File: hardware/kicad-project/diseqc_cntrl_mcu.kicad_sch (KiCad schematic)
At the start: 38 parts, among them IC2 STM32F407VGT6, IC3 USBLC6-2P6, J2 Conn_01x04_Pin, J3 Conn_01x04_Pin, J4 USB4110-GF-A, J5 SWD, Y1 8MHZ

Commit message: Corrective changes to power regulation: F1, PS1
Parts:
- C11, C12, C14, C16, C17, C19, C20, C9, R10, R11, R14, R15, R9: My Stock 50 -> (none)
- C13, C15, C18: My Stock 25 -> (none)
- IC2: footprint STM32:QFP50P1600X1600X160-100N -> diseqc_cntrl:QFP50P1600X1600X160-100N
- IC3: footprint USBCL6:USBLC62P6 -> diseqc_cntrl:USBLC62P6
- J4: footprint USB4110GFA -> diseqc_cntrl:USB4110GFA
- J5: footprint HDRV10W64P254_2X5_1270X495X838P -> diseqc_cntrl:HDRV10W64P254_2X5_1270X495X838P
- NT1: My Stock 1000 -> (none)
- R12, R7, R8: My Stock 0 -> (none)
- R13, R6: My Stock 100 -> (none)
- S1: footprint PCM12SMTBR -> diseqc_cntrl:PCM12SMTBR
- Y1: footprint ABLS 8mhz xtal:ABLS8000MHz20B3HT -> diseqc_cntrl:ABLS8000MHz20B3HT

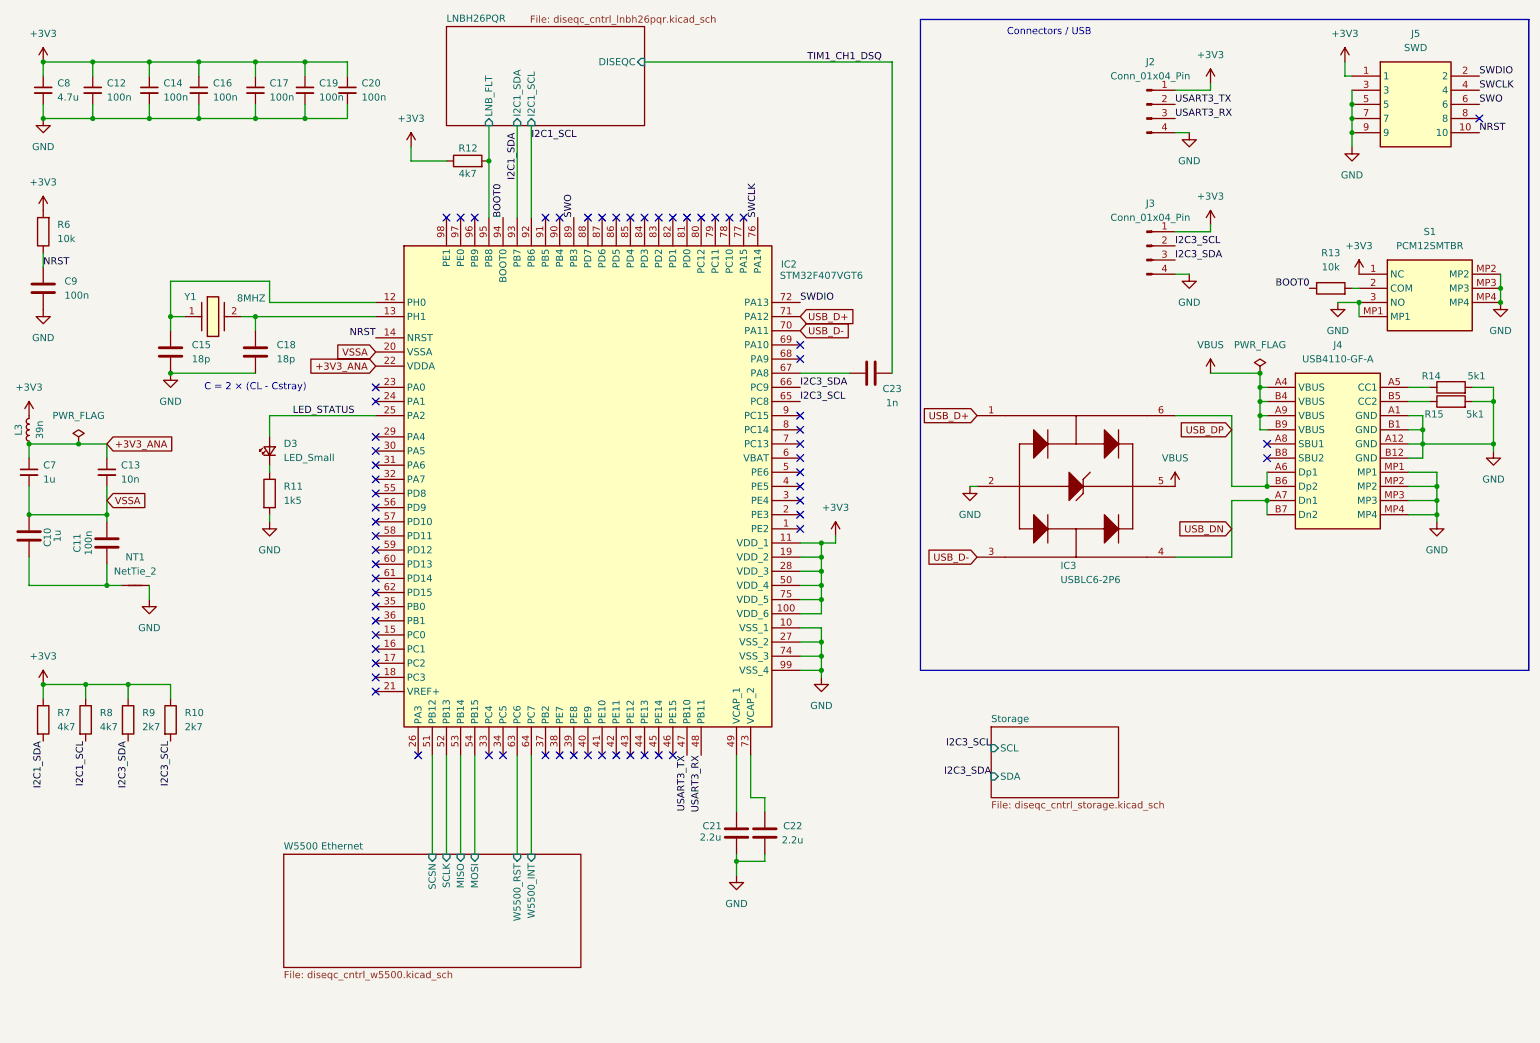
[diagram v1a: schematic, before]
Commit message: Added more test points
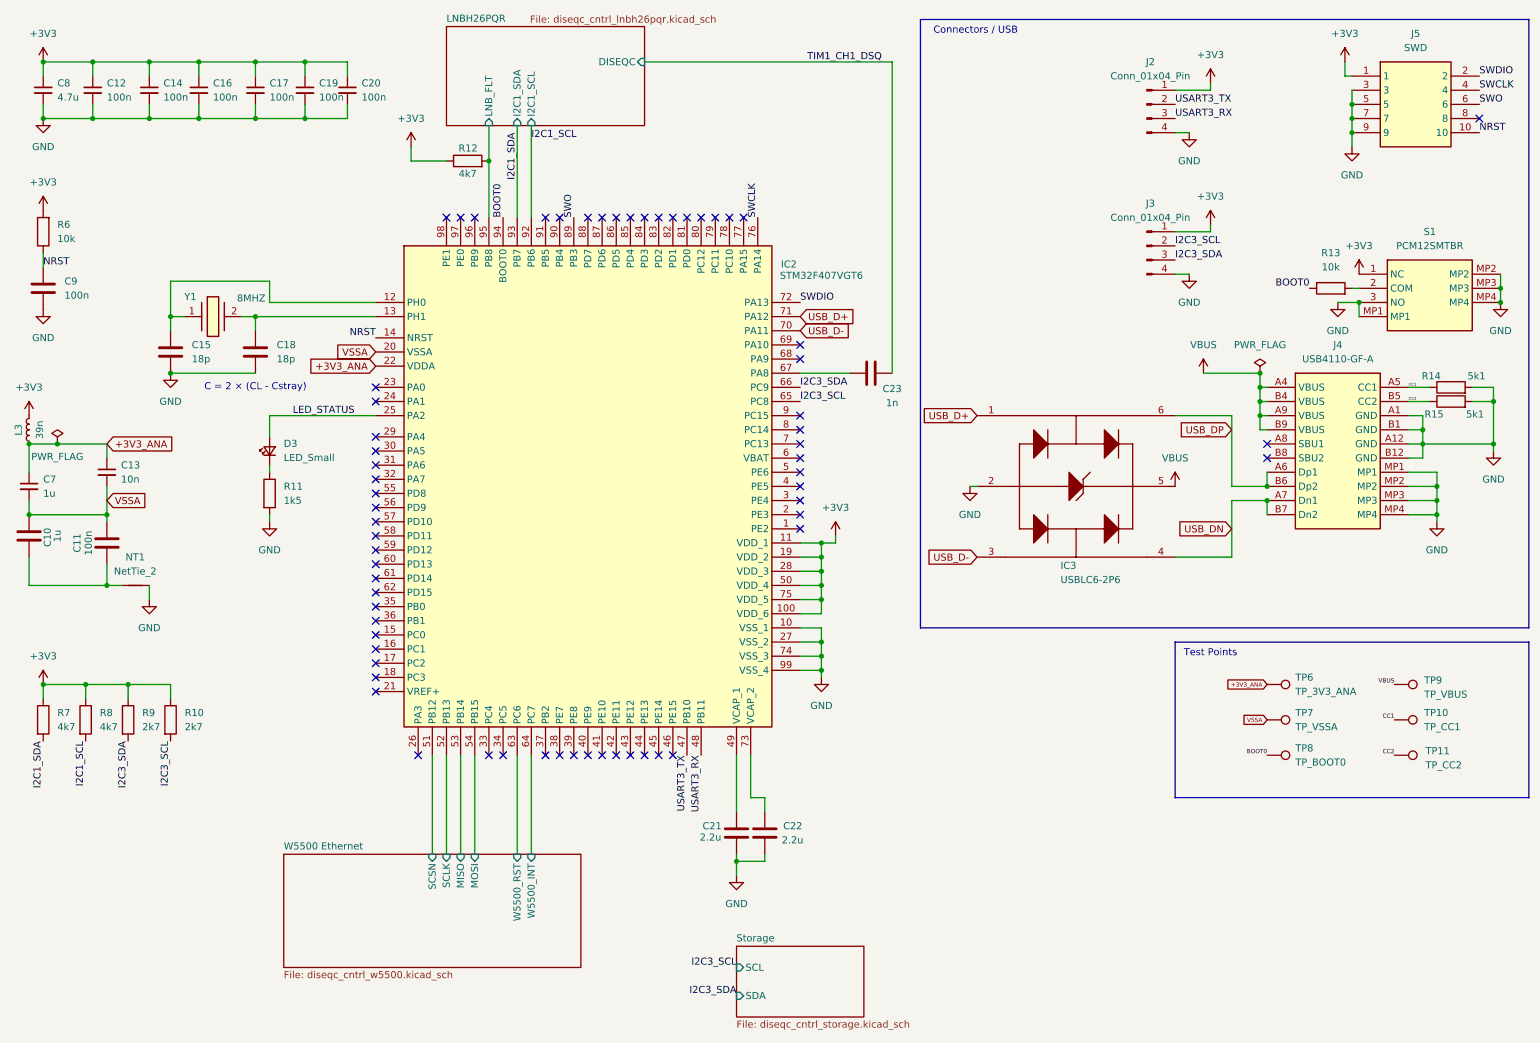
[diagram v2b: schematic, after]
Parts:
- added TP10: TP_CC1, TestPoint:TestPoint_THTPad_D1.0mm_Drill0.5mm, symbol Connector:TestPoint
- added TP11: TP_CC2, TestPoint:TestPoint_THTPad_D1.0mm_Drill0.5mm, symbol Connector:TestPoint
- added TP6: TP_3V3_ANA, TestPoint:TestPoint_THTPad_D1.0mm_Drill0.5mm, symbol Connector:TestPoint
- added TP7: TP_VSSA, TestPoint:TestPoint_THTPad_D1.0mm_Drill0.5mm, symbol Connector:TestPoint
- added TP8: TP_BOOT0, TestPoint:TestPoint_THTPad_D1.0mm_Drill0.5mm, symbol Connector:TestPoint
- added TP9: TP_VBUS, TestPoint:TestPoint_THTPad_D1.0mm_Drill0.5mm, symbol Connector:TestPoint
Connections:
- net +3V3_ANA: now also TP6.1
- net BOOT0: now also TP8.1
- net VBUS: now also TP9.1
- net VSSA: now also TP7.1
- net CC1: now reaches J4.A5 (CC1), R14.1
- net CC1: now also TP10.1
- net CC2: now reaches J4.B5 (CC2), R15.1
- net CC2: now also TP11.1
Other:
- note added: "Test Points"
- moved on the sheet: C7

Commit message: Fixed pin conflict: TIM1_CH1/I2C3_SCL
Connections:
- net TIM1_CH1_DSQ is gone; now on net TIM4_CH1: C23.2
- net I2C3_SCL: now also IC2.67 (PA8); no longer IC2.65 (PC8)
- net LNBH26PQR/DISEQC: now reaches C23.1
- net LNBH26PQR/DISEQC: no longer IC2.67 (PA8)
- net TIM4_CH1: now reaches IC2.59 (PD12)
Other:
- moved on the sheet: C23
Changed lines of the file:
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@@
 	)
 	(no_connect
-		(at 77.47 110.49)
-	)
-	(no_connect
 		(at 77.47 123.19)
 	)
@@
 	)
 	(no_connect
+		(at 153.67 83.82)
+	)
+	(no_connect
 		(at 125.73 50.8)
 	)
@@
 	(wire
 		(pts
-			(xy 170.18 22.86) (xy 125.73 22.86)
-		)
-		(stroke
-			(width 0)
-			(type default)
-		)
-	)
-	(wire
-		(pts
 			(xy 36.83 22.86) (xy 36.83 25.4)
 		)
@@
 	(wire
 		(pts
-			(xy 170.18 78.74) (xy 170.18 22.86)
-		)
-		(stroke
-			(width 0)
-			(type default)
-		)
-	)
-	(wire
-		(pts
 			(xy 236.22 86.36) (xy 237.49 86.36)
 		)
@@
 	(wire
 		(pts
-			(xy 153.67 78.74) (xy 162.56 78.74)
-		)
-		(stroke
-			(width 0)
-			(type default)
-		)
-	)
-	(wire
-		(pts
 			(xy 227.33 27.94) (xy 227.33 26.67)
 		)
@@
 	(wire
 		(pts
+			(xy 125.73 22.86) (xy 129.54 22.86)
+		)
+		(stroke
+			(width 0)
+			(type default)
+		)
+	)
+	(wire
+		(pts
 			(xy 262.89 104.14) (xy 267.97 104.14)
 		)
@@
 		)
 	)
+	(label "TIM4_CH1"
+		(at 77.47 110.49 180)
+		(effects
+			(font
+				(size 1.27 1.27)
+			)
+			(justify right bottom)
+		)
+	)
 	(label "SWCLK"
 		(at 146.05 50.8 90)
@@
 		)
 	)
-	(label "TIM1_CH1_DSQ"
-		(at 154.94 22.86 0)
+	(label "TIM4_CH1"
+		(at 137.16 22.86 0)
 		(effects
 			(font
@@
 		)
 	)
+	(label "I2C3_SCL"
+		(at 153.67 78.74 0)
+		(effects
+			(font
+				(size 1.27 1.27)
+			)
+			(justify left bottom)
+		)
+	)
 	(label "SWCLK"
 		(at 275.59 27.94 0)
@@
 		)
 	)
-	(label "I2C3_SCL"
-		(at 153.67 83.82 0)
-		(effects
-			(font
-				(size 1.27 1.27)
-			)
-			(justify left bottom)
-		)
-	)
 	(label "I2C1_SCL"
 		(at 25.4 144.78 270)
@@
 	(symbol
 		(lib_id "diseqc_cntrl:C")
-		(at 166.37 78.74 90)
+		(at 133.35 22.86 90)
 		(unit 1)
 		(exclude_from_sim no)
@@
 		(dnp no)
 		(property "Reference" "C23"
-			(at 170.18 81.534 90)
+			(at 133.35 26.67 90)
 			(effects
 				(font
@@
 		)
 		(property "Value" "1n"
-			(at 170.18 84.074 90)
+			(at 133.604 28.956 90)
 			(effects
 				(font
@@
 		)
 		(property "Footprint" "Capacitor_SMD:C_0603_1608Metric_Pad1.08x0.95mm_HandSolder"
-			(at 170.18 77.7748 0)
+			(at 137.16 21.8948 0)
 			(effects
 				(font
@@
 		)
 		(property "Datasheet" "https://www.mouser.co.uk/datasheet/3/76/1/GRM188R71H102KA01-01.pdf"
-			(at 166.37 78.74 0)
+			(at 133.35 22.86 0)
 			(effects
 				(font
@@
 		)
 		(property "Description" "Unpolarized capacitor"
-			(at 166.37 78.74 0)
+			(at 133.35 22.86 0)
 			(effects
 				(font
@@
 		)
 		(property "Maufacturer_Part_Number" ""
-			(at 166.37 78.74 90)
+			(at 133.35 22.86 90)
 			(effects
 				(font
@@
 		)
 		(property "Manufacturer_Part_Code" ""
-			(at 166.37 78.74 90)
+			(at 133.35 22.86 90)
 			(effects
 				(font
@@
 		)
 		(property "Mouser_Part_Number" ""
-			(at 166.37 78.74 90)
+			(at 133.35 22.86 90)
 			(effects
 				(font
@@
 		)
 		(property "Mouser Part Number" "81-GRM39X102K050"
-			(at 166.37 78.74 90)
+			(at 133.35 22.86 90)
 			(effects
 				(font
@@
 		)
 		(instances
-			(project ""
+			(project "diseqc_cntrl"
 				(path "/82a905d8-f1d7-4995-9c16-94cf3cdcaad9/65fcf1a0-d0f2-4bf0-9977-67dd9f84afa5"
 					(reference "C23")

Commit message: Moved SWD to TC2050 connector
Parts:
- removed J5: SWD, diseqc_cntrl:HDRV10W64P254_2X5_1270X495X838P, symbol diseqc_cntrl:TSW-105-23-T-D
- added J9: Conn_ARM_SWD_TagConnect_TC2030, Connector:Tag-Connect_TC2050-IDC-NL_2x05_P1.27mm_Vertical, symbol Connector:TC2050
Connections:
- net +3V3: now also J9.1
- net GND: now also J9.3, J9.5, J9.8, J9.9
- net NRST: now also J9.10
- net SWCLK: now also J9.4
- net SWDIO: now also J9.2
- net SWO: now also J9.6
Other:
- moved on the sheet: J2

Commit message: Fix: Add VBUS sense to MCU for USB DFU
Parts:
- added R31: 100k, Resistor_SMD:R_0603_1608Metric_Pad0.98x0.95mm_HandSolder, symbol diseqc_cntrl:R
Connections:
- net +3V3: now also IC2.6 (VBAT)
- net VBUS: now also R31.2
- net VBUS_SENSE: now reaches IC2.68 (PA9)
- net VBUS_SENSE: now also R31.1
- no-connect marks 65 -> 63
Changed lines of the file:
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@@
 	)
 	(no_connect
-		(at 153.67 76.2)
-	)
-	(no_connect
 		(at 140.97 50.8)
 	)
@@
 	)
 	(no_connect
-		(at 153.67 93.98)
-	)
-	(no_connect
 		(at 77.47 135.89)
 	)
@@
 	(wire
 		(pts
+			(xy 172.72 76.2) (xy 172.72 73.66)
+		)
+		(stroke
+			(width 0)
+			(type default)
+		)
+	)
+	(wire
+		(pts
 			(xy 147.32 166.37) (xy 142.24 166.37)
 		)
@@
 	(wire
 		(pts
+			(xy 171.45 76.2) (xy 172.72 76.2)
+		)
+		(stroke
+			(width 0)
+			(type default)
+		)
+	)
+	(wire
+		(pts
 			(xy 15.24 101.6) (xy 15.24 104.14)
 		)
@@
 	(wire
 		(pts
+			(xy 157.48 93.98) (xy 157.48 109.22)
+		)
+		(stroke
+			(width 0)
+			(type default)
+		)
+	)
+	(wire
+		(pts
 			(xy 36.83 33.02) (xy 45.72 33.02)
 		)
@@
 	(wire
 		(pts
+			(xy 153.67 76.2) (xy 163.83 76.2)
+		)
+		(stroke
+			(width 0)
+			(type default)
+		)
+	)
+	(wire
+		(pts
 			(xy 15.24 91.44) (xy 15.24 96.52)
 		)
@@
 	(wire
 		(pts
+			(xy 153.67 93.98) (xy 157.48 93.98)
+		)
+		(stroke
+			(width 0)
+			(type default)
+		)
+	)
+	(wire
+		(pts
 			(xy 102.87 147.32) (xy 102.87 165.1)
 		)
@@
 		)
 	)
+	(label "VBUS_SENSE"
+		(at 153.67 76.2 0)
+		(effects
+			(font
+				(size 0.508 0.508)
+			)
+			(justify left bottom)
+		)
+	)
 	(label "NRST"
 		(at 77.47 72.39 180)
@@
 	)
 	(symbol
+		(lib_id "diseqc_cntrl:VBUS")
+		(at 172.72 73.66 0)
+		(unit 1)
+		(exclude_from_sim no)
+		(in_bom yes)
+		(on_board yes)
+		(dnp no)
+		(fields_autoplaced yes)
+		(property "Reference" "#PWR033"
+			(at 172.72 77.47 0)
+			(effects
+				(font
+					(size 1.27 1.27)
+				)
+				(hide yes)
+			)
+		)
+		(property "Value" "VBUS"
+			(at 172.72 68.58 0)
+			(effects
+				(font
+					(size 1.27 1.27)
+				)
+			)
+		)
+		(property "Footprint" ""
+			(at 172.72 73.66 0)
+			(effects
+				(font
+					(size 1.27 1.27)
+				)
+				(hide yes)
+			)
+		)
+		(property "Datasheet" ""
+			(at 172.72 73.66 0)
+			(effects
+				(font
+					(size 1.27 1.27)
+				)
+				(hide yes)
+			)
+		)
+		(property "Description" "Power symbol creates a global label with name \"VBUS\""
+			(at 172.72 73.66 0)
+			(effects
+				(font
+					(size 1.27 1.27)
+				)
+				(hide yes)
+			)
+		)
+		(pin "1"
+		)
+		(instances
+			(project "diseqc_cntrl"
+				(path "/82a905d8-f1d7-4995-9c16-94cf3cdcaad9/65fcf1a0-d0f2-4bf0-9977-67dd9f84afa5"
+					(reference "#PWR033")
+					(unit 1)
+				)
+			)
+		)
+	)
+	(symbol
 		(lib_id "diseqc_cntrl:+3V3")
 		(at 17.78 22.86 0)
@@
 					(unit 1)
 				)
+			)
+		)
+	)
+	(symbol
+		(lib_id "diseqc_cntrl:R")
+		(at 167.64 76.2 90)
+		(unit 1)
+		(exclude_from_sim no)
+		(in_bom yes)
+		(on_board yes)
+		(dnp no)
+		(fields_autoplaced yes)
+		(property "Reference" "R31"
+			(at 167.64 69.85 90)
+			(effects
+				(font
+					(size 1.27 1.27)
+				)
+			)
+		)
+		(property "Value" "100k"
+			(at 167.64 72.39 90)
+			(effects
+				(font
+					(size 1.27 1.27)
+				)
+			)
+		)
+		(property "Footprint" "Resistor_SMD:R_0603_1608Metric_Pad0.98x0.95mm_HandSolder"
+			(at 167.64 77.978 90)
+			(effects
+				(font
+					(size 1.27 1.27)
+				)
+				(hide yes)
+			)
+		)
+		(property "Datasheet" "https://www.mouser.com/catalog/specsheets/YAGEO_PYu_RC_Group_51_RoHS_L_12.pdf"
+			(at 167.64 76.2 0)
+			(effects
+				(font
+					(size 1.27 1.27)
+				)
+				(hide yes)
+			)
+		)
+		(property "Description" "Resistor"
+			(at 167.64 76.2 0)
+			(effects
+				(font
+					(size 1.27 1.27)
+				)
+				(hide yes)
+			)
+		)
+		(property "Mouser Part Number" "603-RC0603JR-07100KL"
+			(at 167.64 76.2 0)
+			(effects
+				(font
+					(size 1.27 1.27)
+				)
+				(hide yes)
+			)
+		)
+		(pin "1"
+		)
+		(pin "2"
+		)
+		(instances
+			(project ""
+				(path "/82a905d8-f1d7-4995-9c16-94cf3cdcaad9/65fcf1a0-d0f2-4bf0-9977-67dd9f84afa5"
+					(reference "R31")
+					(unit 1)
+				)

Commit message: Added USB-UART instead of board headers
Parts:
- removed J2: Conn_01x04_Pin, Connector_PinHeader_2.00mm:PinHeader_1x04_P2.00mm_Vertical_SMD_Pin1Left, symbol diseqc_cntrl:Conn_01x04_Pin
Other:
- added sheet USB-UART (diseqc_cntrl_usb.kicad_sch)
- moved on the sheet: J3

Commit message: WIP: checkpoint mailbox interop investigation
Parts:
- J9: value Conn_ARM_SWD_TagConnect_TC2030 -> Conn_ARM_SWD_TagConnect_TC2050; footprint Connector:Tag-Connect_TC2050-IDC-NL_2x05_P1.27mm_Vertical -> Connector:Tag-Connect_TC2050-IDC-FP_2x05_P1.27mm_Vertical
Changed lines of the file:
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@@
 	)
 	(junction
-		(at 255.27 33.02)
-		(diameter 0)
-		(color 0 0 0 0)
-	)
-	(junction
 		(at 279.4 63.5)
 		(diameter 0)
@@
 			)
 		)
-		(property "Value" "Conn_ARM_SWD_TagConnect_TC2030"
+		(property "Value" "Conn_ARM_SWD_TagConnect_TC2050"
 			(at 248.92 20.32 0)
 			(effects
@@
 			)
 		)
-		(property "Footprint" "Connector:Tag-Connect_TC2050-IDC-NL_2x05_P1.27mm_Vertical"
+		(property "Footprint" "Connector:Tag-Connect_TC2050-IDC-FP_2x05_P1.27mm_Vertical"
 			(at 248.92 33.02 0)
 			(effects

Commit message: Freezing hardware v0.3
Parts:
- C9: value 100n -> 4.7n; now not fitted
- J9: symbol Connector:TC2050 -> Tag-Connect:TC2050-IDC_Cortex-M; now in the parts list
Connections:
- net GND: now also J9.7 ((key)); no longer J9.8
